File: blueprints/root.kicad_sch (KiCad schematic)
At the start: 1 part, among them U1 ESP32-S3

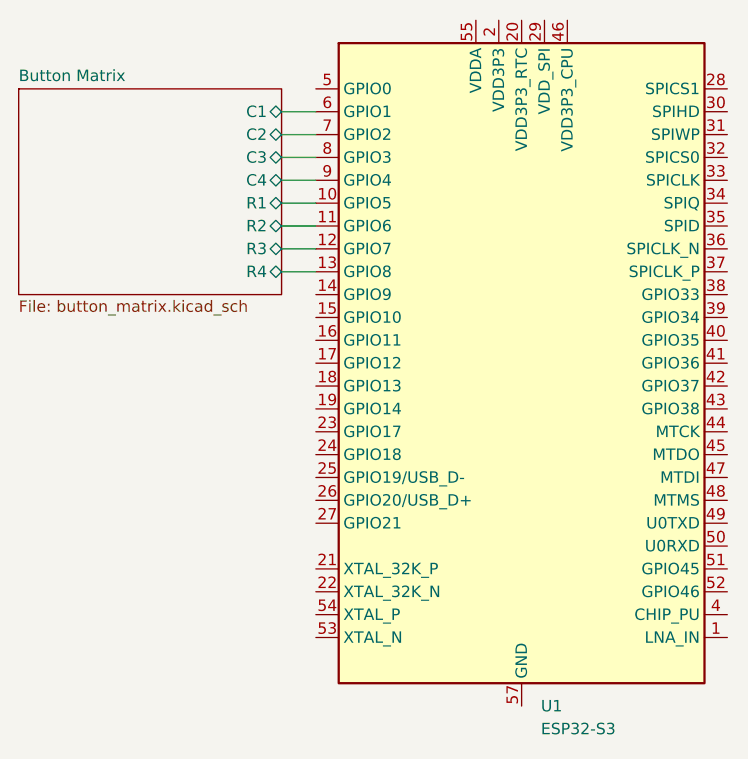
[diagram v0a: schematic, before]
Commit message: refactor: Change button matrix diodes form factor
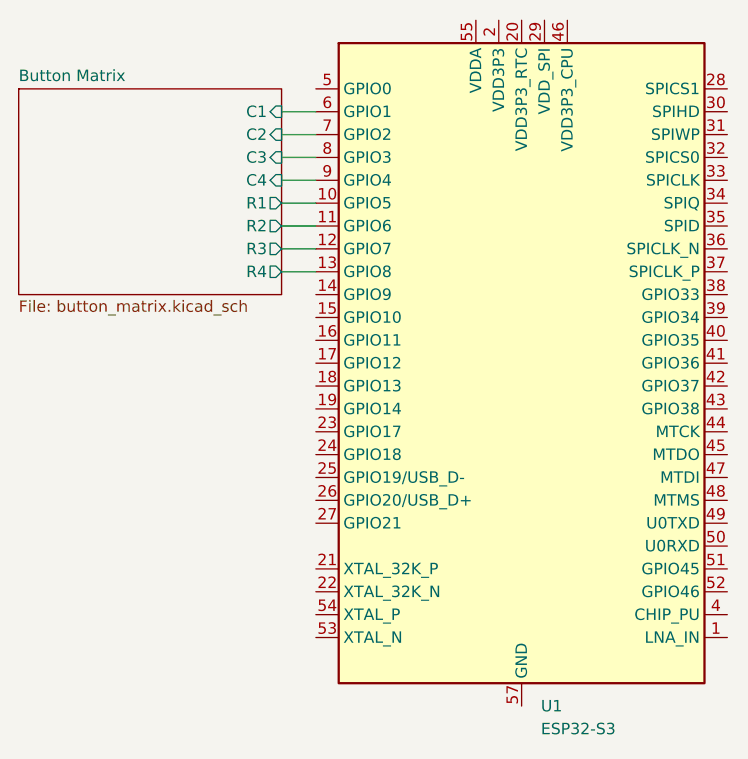
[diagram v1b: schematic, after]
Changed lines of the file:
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@@
 			)
 		)
-		(pin "C1" bidirectional
+		(pin "C1" input
 			(at 180.34 102.87 0)
 			(effects
@@
 			)
 		)
-		(pin "C2" bidirectional
+		(pin "C2" input
 			(at 180.34 105.41 0)
 			(effects
@@
 			)
 		)
-		(pin "C3" bidirectional
+		(pin "C3" input
 			(at 180.34 107.95 0)
 			(effects
@@
 			)
 		)
-		(pin "C4" bidirectional
+		(pin "C4" input
 			(at 180.34 110.49 0)
 			(effects
@@
 			)
 		)
-		(pin "R1" bidirectional
+		(pin "R1" output
 			(at 180.34 113.03 0)
 			(effects
@@
 			)
 		)
-		(pin "R2" bidirectional
+		(pin "R2" output
 			(at 180.34 115.57 0)
 			(effects
@@
 			)
 		)
-		(pin "R3" bidirectional
+		(pin "R3" output
 			(at 180.34 118.11 0)
 			(effects
@@
 			)
 		)
-		(pin "R4" bidirectional
+		(pin "R4" output
 			(at 180.34 120.65 0)
 			(effects
